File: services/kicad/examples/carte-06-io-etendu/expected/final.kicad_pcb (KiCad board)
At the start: 2 copper layers, 47.4 x 36.3 mm, 35 parts, among them J1 IN_5V, J10 IO0, J11 IO1, J2 SWD, U1 STM32F103C8T6, U2 AMS1117-3.3

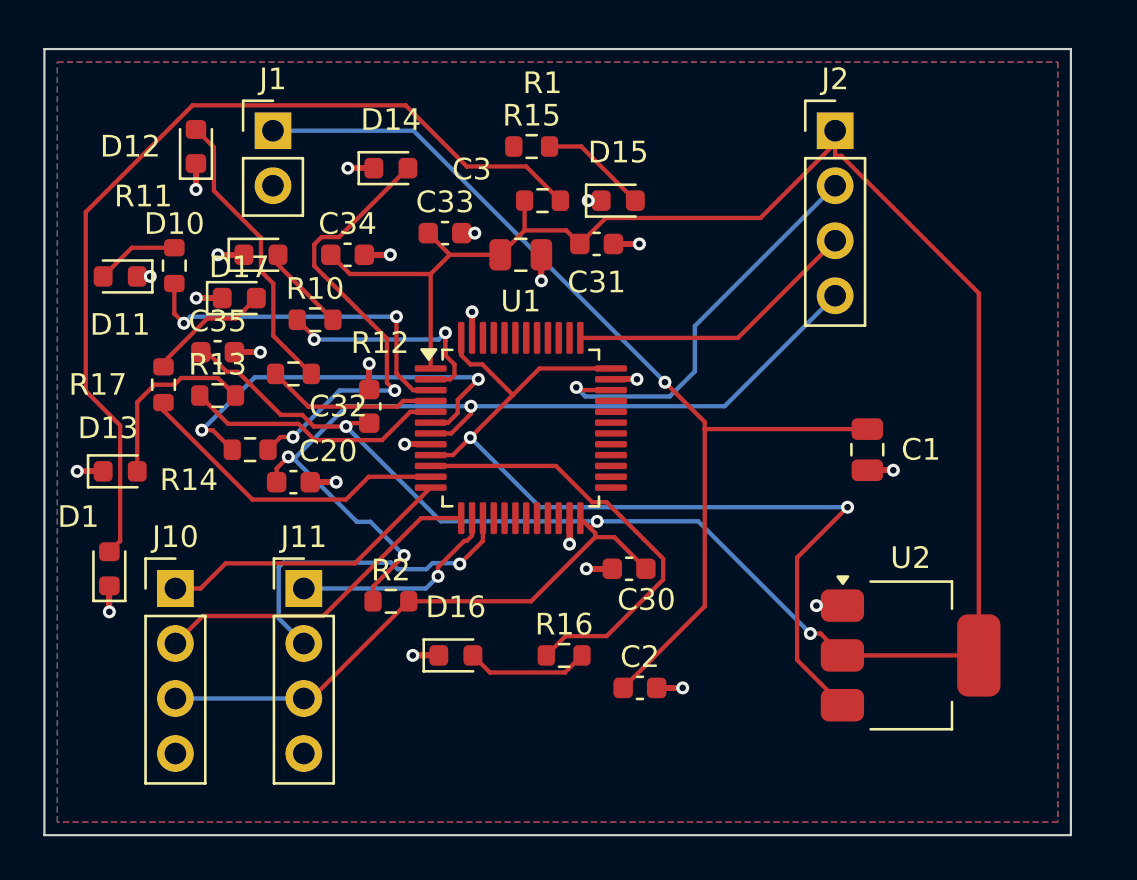
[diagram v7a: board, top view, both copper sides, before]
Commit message: fix(banc): le banc route comme la production — plafond 8, budget du client
D-2026-09-24-f. run_pipeline.py prenait 2 couches et 1800 s par défaut, et
carte-07 écrivait 2 en dur : dix cartes sur quinze ne pouvaient jamais
escalader, et la règle « toute connexion manquante fait monter » était
inerte dans le banc. Mesuré sur carte-07 : 97 %, seule la masse manquante,
« le palier suivant sera tenté »… puis retour à 2 couches.

Plafond par défaut 8 (client Pro Max), budget min(600 + 300 x plafond, 3600)
comme routingSearchBudgetS côté client. En production, rien ne change : le
plafond reste celui du plan.

Livraisons du jour, toutes vérifiées par kicad-cli et contre le schéma
(0 erreur bloquante, 0 connexion manquante, 0 court-circuit) :
carte-04, 05, 06, 08 (campagne de l'après-midi) et carte-09, 10 (4 couches).
Les boards versionnés de ces cartes court-circuitaient des nets du schéma.

Correction de ma propre erreur dans la doc : carte-07 n'avait jamais
escaladé ; les lignes « palier 4 et 6 » du journal étaient celles de
carte-08, démarrée la même minute.

Co-Authored-By: Claude Opus 5.5 <noreply@anthropic.com>
Claude-Session: https://claude.ai/code/session_01TnMqm4La2CxQHHB5K8aSSV
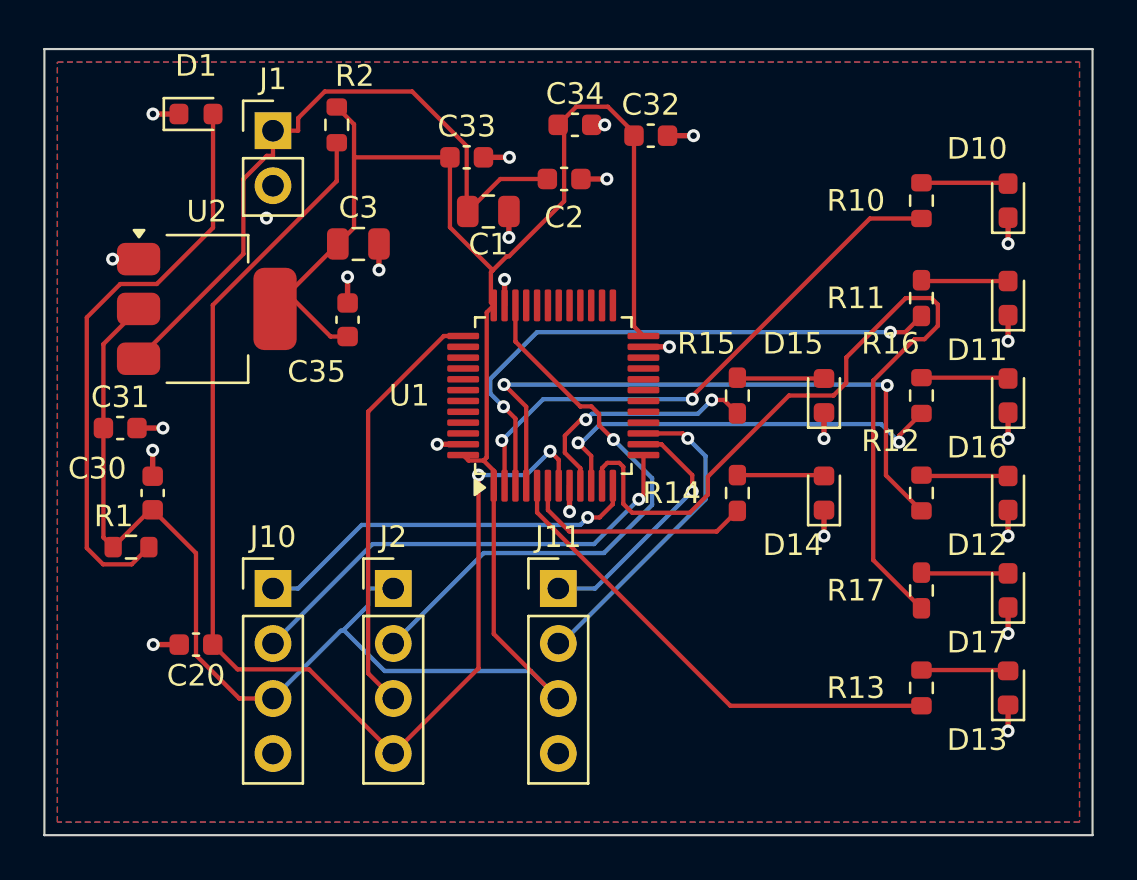
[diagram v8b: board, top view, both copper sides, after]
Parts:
- moved D13 42.2 mm to (153.0, 104.5), turned to 90 degrees
- moved D11 41.0 mm to (153.0, 86.5), turned to 90 degrees
- moved D12 40.8 mm to (153.0, 95.5)
- moved D17 38.0 mm to (153.0, 100.0), turned to 90 degrees
- moved R17 36.3 mm to (149.0, 100.0)
- moved U2 36.2 mm to (116.0, 87.0)
- moved R13 35.2 mm to (149.0, 104.5), turned to 90 degrees
- moved D10 34.6 mm to (153.0, 82.0), turned to 90 degrees
- moved R11 34.5 mm to (149.0, 86.5)
- moved R12 29.5 mm to (149.0, 95.5), turned to 90 degrees
- moved J2 29.4 mm to (124.6, 99.9)
- moved R10 28.5 mm to (149.0, 82.0), turned to 90 degrees
- moved D16 28.2 mm to (153.0, 91.0), turned to 90 degrees
- moved D14 25.0 mm to (144.5, 95.5), turned to 90 degrees
- moved R1 24.8 mm to (112.5, 98.0)
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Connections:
- U1 pad 36: PWR_FLAG -> +3V3
- U1 pad 48: PWR_FLAG -> +3V3
- U1 pad 9: PWR_FLAG -> IO_L5
- U2 pad 3: PWR_FLAG -> VIN
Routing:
- net GND: track 87.0 -> 28.2 mm, vias 24 -> 25
- net PWR_FLAG: track 43.7 -> 0.00 mm, vias 2 -> 0
- net IO_L7: track 14.8 -> 40.2 mm
- net IO_L2: track 7.90 -> 29.3 mm, vias 0 -> 2
- net LEDA4: track 21.1 -> 4.02 mm, vias 2 -> 0
- net LED_PWR: track 42.3 -> 27.0 mm
- net +3V3: track 130.9 -> 115.7 mm, vias 3 -> 0
- net VIN: track 46.9 -> 31.7 mm, vias 1 -> 0
- net IO_L0: track 10.7 -> 25.8 mm
- net NRST: track 42.0 -> 56.0 mm, vias 3 -> 2
- net IO_L5: track 0.00 -> 11.5 mm, vias 0 -> 2
- net IO_L3: track 12.1 -> 22.7 mm
- net IO_L1: track 16.5 -> 26.5 mm
- net LEDA2: track 13.5 -> 4.02 mm
- net IO_L4: track 19.0 -> 10.7 mm, vias 2 -> 0
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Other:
- board size 47.4 x 36.3 mm -> 48.4 x 36.3 mm
